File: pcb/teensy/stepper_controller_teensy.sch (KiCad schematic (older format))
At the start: 15 parts, among them P1 HEADER_02X08_SMD, SW1 SPST_SLIDE_AS, U1 TLE7230R

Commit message: Added L6470.
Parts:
- removed C2: 0.1uF, stepper_controller_teensy:SM1210, symbol 0.1uF
- removed L2, L3, L4, L5, L6, L7, L8, L9: LED_24V, stepper_controller_teensy:LED_555-3XXX, symbol LED_24V
- removed P1: HEADER_02X08_SMD, stepper_controller_teensy:HEADER_02x08_SMD, symbol HEADER_02X08_SMD
- removed U1: TLE7230R, stepper_controller_teensy:PG-DSO-36, symbol TLE7230R
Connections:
- net labels removed: OUT0, OUT1, OUT2, OUT3, OUT4, OUT5, OUT6, OUT7
- wire segments 85 -> 21
- no-connect marks 25 -> 23

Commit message: Added TERM_BLK_ANG_4_PIN.
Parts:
- added U?: L6470, footprints:POWERSO-36, symbol L6470
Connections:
- net labels added: BUSY, FLAG, OUT1A, OUT1B, OUT2A, OUT2B, SW
- net labels removed: PWM
- wire segments 21 -> 50
- no-connect marks 23 -> 24
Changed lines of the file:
@@
 NoConn ~ 3850 1150
 NoConn ~ 1350 1050
-NoConn ~ 1350 1450
 NoConn ~ 1350 1550
 NoConn ~ 1350 1650
@@
 RESET
 Text Label 1050 1350 0    60   ~ 0
-PWM
+FLAG
 $Comp
 L LED_24V L1
@@
 	1    0    0    -1
 $EndComp
+$Comp
+L L6470 U?
+U 1 1 57AA1BBB
+P 7200 3200
+F 0 "U?" H 7700 2300 60  0000 C CNN
+F 1 "L6470" H 6800 2300 60  0000 C CNN
+F 2 "footprints:POWERSO-36" H 7200 4850 60  0001 C CNN
+F 3 "" H 7600 3700 60  0000 C CNN
+F 4 "digikey" H 7200 4750 60  0001 C CNN "Vendor"
+F 5 "497-16432-1-ND" H 7200 4950 60  0001 C CNN "PartNumber"
+F 6 "Bipolar Motor Driver DMOS SPI PowerSO-36" H 7200 5050 60  0001 C CNN "Description"
+	1    7200 3200
+	1    0    0    -1
+$EndComp
+Wire Wire Line
+	6550 3250 6250 3250
+Wire Wire Line
+	6550 3350 6250 3350
+Wire Wire Line
+	6550 3450 6250 3450
+Wire Wire Line
+	6550 3550 6250 3550
+Text Label 6250 3450 0    60   ~ 0
+MISO
+Text Label 6250 3550 0    60   ~ 0
+MOSI
+Text Label 6250 3350 0    60   ~ 0
+SCK
+Text Label 6250 3250 0    60   ~ 0
+CS
+NoConn ~ 7850 3750
+NoConn ~ 6550 3750
+$Comp
+L GND #PWR?
+U 1 1 57AA211F
+P 7250 4300
+F 0 "#PWR?" H 7250 4050 50  0001 C CNN
+F 1 "GND" H 7255 4127 50  0000 C CNN
+F 2 "" H 7250 4300 50  0000 C CNN
+F 3 "" H 7250 4300 50  0000 C CNN
+	1    7250 4300
+	1    0    0    -1
+$EndComp
+Wire Wire Line
+	7050 4150 7050 4200
+Wire Wire Line
+	7050 4200 7450 4200
+Wire Wire Line
+	7450 4200 7450 4150
+Wire Wire Line
+	7150 4150 7150 4200
+Connection ~ 7150 4200
+Wire Wire Line
+	7250 4150 7250 4300
+Connection ~ 7250 4200
+Wire Wire Line
+	7350 4150 7350 4200
+Connection ~ 7350 4200
+Wire Wire Line
+	7850 2950 7950 2950
+Wire Wire Line
+	7850 3150 7950 3150
+Wire Wire Line
+	7850 3350 7950 3350
+Wire Wire Line
+	7850 3550 7950 3550
+Wire Wire Line
+	7850 3050 7900 3050
+Wire Wire Line
+	7900 3050 7900 2950
+Connection ~ 7900 2950
+Wire Wire Line
+	7850 3250 7900 3250
+Wire Wire Line
+	7900 3250 7900 3150
+Connection ~ 7900 3150
+Wire Wire Line
+	7850 3450 7900 3450
+Wire Wire Line
+	7900 3450 7900 3350
+Connection ~ 7900 3350
+Wire Wire Line
+	7850 3650 7900 3650
+Wire Wire Line
+	7900 3650 7900 3550
+Connection ~ 7900 3550
+Text Label 7950 2950 0    60   ~ 0
+OUT1A
+Text Label 7950 3150 0    60   ~ 0
+OUT2A
+Text Label 7950 3350 0    60   ~ 0
+OUT1B
+Text Label 7950 3550 0    60   ~ 0
+OUT2B
+Wire Wire Line
+	6550 3150 6250 3150
+Text Label 6250 3150 0    60   ~ 0
+RESET
+$Comp
+L GND #PWR?
+U 1 1 57AA2829
+P 6050 3100
+F 0 "#PWR?" H 6050 2850 50  0001 C CNN
+F 1 "GND" H 6055 2927 50  0000 C CNN
+F 2 "" H 6050 3100 50  0000 C CNN
+F 3 "" H 6050 3100 50  0000 C CNN
+	1    6050 3100
+	1    0    0    -1
+$EndComp
+Wire Wire Line
+	6550 3050 6050 3050
+Wire Wire Line
+	6050 3050 6050 3100
+Wire Wire Line
+	6550 2950 6250 2950
+Text Label 6250 2950 0    60   ~ 0
+BUSY
+Wire Wire Line
+	6550 2850 6250 2850
+Text Label 6250 2850 0    60   ~ 0
+FLAG
+Wire Wire Line
+	1350 1450 1050 1450
+Text Label 1050 1450 0    60   ~ 0
+BUSY
+Wire Wire Line
+	6550 3650 6250 3650
+Text Label 6250 3650 0    60   ~ 0
+SW
 $EndSCHEMATC

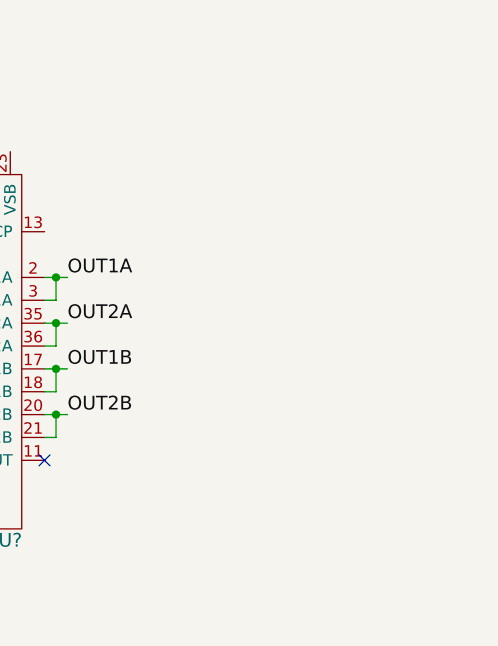
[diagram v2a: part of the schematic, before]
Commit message: Added terminal blocks.
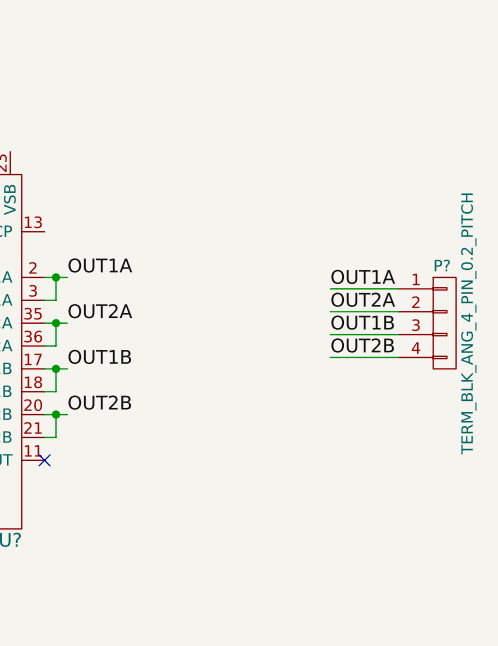
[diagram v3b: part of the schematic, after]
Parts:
- added P?: TERM_BLK_ANG_4_PIN_0.2_PITCH, footprints:TERM_BLK_ANG_4_PIN_0.2_PITCH, symbol TERM_BLK_ANG_4_PIN_0.2_PITCH
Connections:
- wire segments 50 -> 54
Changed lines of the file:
@@
 Text Label 6250 3650 0    60   ~ 0
 SW
+Wire Wire Line
+	9400 3000 9100 3000
+Wire Wire Line
+	9400 3100 9100 3100
+Wire Wire Line
+	9400 3200 9100 3200
+Wire Wire Line
+	9400 3300 9100 3300
+Text Label 9100 3000 0    60   ~ 0
+OUT1A
+Text Label 9100 3100 0    60   ~ 0
+OUT2A
+Text Label 9100 3200 0    60   ~ 0
+OUT1B
+Text Label 9100 3300 0    60   ~ 0
+OUT2B
+$Comp
+L TERM_BLK_ANG_4_PIN_0.2_PITCH P?
+U 1 1 57AA5C55
+P 9600 3150
+F 0 "P?" H 9550 3400 50  0000 L CNN
+F 1 "TERM_BLK_ANG_4_PIN_0.2_PITCH" V 9700 3150 50  0000 C CNN
+F 2 "footprints:TERM_BLK_ANG_4_PIN_0.2_PITCH" H 9500 3300 50  0001 C CNN
+F 3 "" H 9600 3150 50  0000 C CNN
+F 4 "digikey" H 9700 3500 60  0001 C CNN "Vendor"
+F 5 "A98350-ND" H 9800 3600 60  0001 C CNN "PartNumber"
+F 6 "TERM BLOCK 4POS 35DEG 5.08MM" H 9900 3700 60  0001 C CNN "Description"
+	1    9600 3150
+	1    0    0    -1
+$EndComp
 $EndSCHEMATC

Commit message: Added components and footprints.
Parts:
- removed C1: 10uF, stepper_controller_teensy:SM1210, symbol 10uF
- removed L1: LED_24V, stepper_controller_teensy:LED_555-3XXX, symbol LED_24V
- added SW?: KT_SWITCH, footprints:KT_SWITCH, symbol KT_SWITCH
- added T?: TERM_BLK_2_PIN_0.1_PITCH, footprints:TERM_BLK_2_PIN_0.1_PITCH, symbol TERM_BLK_2_PIN_0.1_PITCH
- added U?: MAX6817, footprints:MAX6817, symbol MAX6817
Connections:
- net labels added: +3.3V, SW_B
- net labels removed: VEE
- wire segments 54 -> 57
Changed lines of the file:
@@
 Wire Wire Line
 	1050 850  1350 850
-$Comp
-L VEE #PWR03
-U 1 1 57715626
-P 4350 800
-F 0 "#PWR03" H 4350 650 50  0001 C CNN
-F 1 "VEE" H 4367 973 50  0000 C CNN
-F 2 "" H 4350 800 50  0000 C CNN
-F 3 "" H 4350 800 50  0000 C CNN
-	1    4350 800
-	1    0    0    -1
-$EndComp
-Wire Wire Line
-	3850 950  4650 950
-Wire Wire Line
-	4350 950  4350 800
 NoConn ~ 3850 850
 NoConn ~ 3850 1050
-NoConn ~ 3850 1150
 NoConn ~ 1350 1050
 NoConn ~ 1350 1550
@@
 FLAG
 $Comp
-L LED_24V L1
-U 1 1 578D4B9A
-P 3700 3150
-F 0 "L1" H 3750 3250 50  0000 C CNN
-F 1 "LED_24V" H 3750 3050 50  0000 C CNN
-F 2 "stepper_controller_teensy:LED_555-3XXX" H 3600 3150 60  0001 C CNN
-F 3 "" H 3700 3150 60  0000 C CNN
-F 4 "digikey" H 3800 3350 60  0001 C CNN "Vendor"
-F 5 "350-1723-ND" H 3900 3450 60  0001 C CNN "PartNumber"
-F 6 "LED 2MM 24V VERTICAL RED PC MNT" H 4000 3550 60  0001 C CNN "Description"
-	1    3700 3150
-	0    1    1    0
-$EndComp
-$Comp
 L SPST_SLIDE_AS SW1
 U 1 1 578D4BFB
@@
 	0    1    1    0
 $EndComp
-$Comp
-L VDD #PWR07
-U 1 1 578D4F9D
-P 3100 2900
-F 0 "#PWR07" H 3100 2750 50  0001 C CNN
-F 1 "VDD" H 3117 3073 50  0000 C CNN
-F 2 "" H 3100 2900 50  0000 C CNN
-F 3 "" H 3100 2900 50  0000 C CNN
-	1    3100 2900
-	1    0    0    -1
-$EndComp
 Wire Wire Line
 	3100 2900 3100 2950
@@
 Text Label 3100 3550 0    60   ~ 0
 LED_PWR
-$Comp
-L GND #PWR08
-U 1 1 578D534F
-P 3700 3400
-F 0 "#PWR08" H 3700 3150 50  0001 C CNN
-F 1 "GND" H 3705 3227 50  0000 C CNN
-F 2 "" H 3700 3400 50  0000 C CNN
-F 3 "" H 3700 3400 50  0000 C CNN
-	1    3700 3400
-	1    0    0    -1
-$EndComp
-Wire Wire Line
-	3700 3350 3700 3400
-Wire Wire Line
-	3700 2950 3700 2850
-Text Label 3700 2850 0    60   ~ 0
-LED_PWR
-$Comp
-L 10uF C1
-U 1 1 578FA17B
-P 2500 3200
-F 0 "C1" H 2550 3300 40  0000 L CNN
-F 1 "10uF" H 2550 3100 30  0000 L CNN
-F 2 "stepper_controller_teensy:SM1210" H 2538 3050 30  0001 C CNN
-F 3 "" H 2500 3200 60  0000 C CNN
-F 4 "digikey" H 2600 3400 60  0001 C CNN "Vendor"
-F 5 "445-4536-1-ND" H 2700 3500 60  0001 C CNN "PartNumber"
-F 6 "CAP CER 10UF 50V 10% X7S 1210" H 2800 3600 60  0001 C CNN "Description"
-	1    2500 3200
-	1    0    0    -1
-$EndComp
-$Comp
-L GND #PWR09
-U 1 1 578FA28E
-P 2500 3450
-F 0 "#PWR09" H 2500 3200 50  0001 C CNN
-F 1 "GND" H 2505 3277 50  0000 C CNN
-F 2 "" H 2500 3450 50  0000 C CNN
-F 3 "" H 2500 3450 50  0000 C CNN
-	1    2500 3450
-	1    0    0    -1
-$EndComp
-$Comp
-L VDD #PWR010
-U 1 1 578FA2C6
-P 2500 2900
-F 0 "#PWR010" H 2500 2750 50  0001 C CNN
-F 1 "VDD" H 2517 3073 50  0000 C CNN
-F 2 "" H 2500 2900 50  0000 C CNN
-F 3 "" H 2500 2900 50  0000 C CNN
-	1    2500 2900
-	1    0    0    -1
-$EndComp
-Wire Wire Line
-	2500 2900 2500 3000
-Wire Wire Line
-	2500 3400 2500 3450
 $Comp
 L PWR_FLAG #FLG011
@@
 L PWR_FLAG #FLG013
 U 1 1 578F9241
-P 4650 800
-F 0 "#FLG013" H 4650 895 50  0001 C CNN
-F 1 "PWR_FLAG" H 4650 1024 50  0000 C CNN
-F 2 "" H 4650 800 50  0000 C CNN
-F 3 "" H 4650 800 50  0000 C CNN
-	1    4650 800
-	1    0    0    -1
-$EndComp
-Wire Wire Line
-	4650 950  4650 800
-Connection ~ 4350 950
+P 4400 1000
+F 0 "#FLG013" H 4400 1095 50  0001 C CNN
+F 1 "PWR_FLAG" H 4400 1224 50  0000 C CNN
+F 2 "" H 4400 1000 50  0000 C CNN
+F 3 "" H 4400 1000 50  0000 C CNN
+	1    4400 1000
+	1    0    0    -1
+$EndComp
 Wire Wire Line
 	1050 800  1050 850
@@
 	1    0    0    -1
 $EndComp
+$Comp
+L TERM_BLK_2_PIN_0.1_PITCH T?
+U 1 1 57AB3CB0
+P 9600 4400
+F 0 "T?" H 9600 4550 50  0000 C CNN
+F 1 "TERM_BLK_2_PIN_0.1_PITCH" V 9700 4400 50  0000 C CNN
+F 2 "footprints:TERM_BLK_2_PIN_0.1_PITCH" H 9500 4450 60  0001 C CNN
+F 3 "" H 9600 4400 60  0000 C CNN
+F 4 "digikey" H 9700 4650 60  0001 C CNN "Vendor"
+F 5 "A98333-ND" H 9800 4750 60  0001 C CNN "PartNumber"
+F 6 "TERM BLOCK 2POS SIDE ENT 2.54MM" H 9900 4850 60  0001 C CNN "Description"
+	1    9600 4400
+	1    0    0    -1
+$EndComp
+$Comp
+L GND #PWR?
+U 1 1 57AB53B5
+P 9350 4500
+F 0 "#PWR?" H 9350 4250 50  0001 C CNN
+F 1 "GND" H 9355 4327 50  0000 C CNN
+F 2 "" H 9350 4500 50  0000 C CNN
+F 3 "" H 9350 4500 50  0000 C CNN
+	1    9350 4500
+	1    0    0    -1
+$EndComp
+Text Label 1600 4400 0    60   ~ 0
+SW_B
+$Comp
+L KT_SWITCH SW?
+U 1 1 57AB5A65
+P 2250 5500
+F 0 "SW?" H 2250 5450 40  0000 C CNN
+F 1 "KT_SWITCH" H 2250 5600 40  0000 C CNN
+F 2 "footprints:KT_SWITCH" H 2150 5300 60  0001 C CNN
+F 3 "" H 2250 5450 60  0000 C CNN
+F 4 "digikey" H 2350 5700 60  0001 C CNN "Vendor"
+F 5 "CKN1860CT-ND" H 2450 5800 60  0001 C CNN "PartNumber"
+F 6 "SWITCH TACTILE SPST-NO 1VA 32V" H 2550 5900 60  0001 C CNN "Description"
+	1    2250 5500
+	0    1    1    0
+$EndComp
+Wire Wire Line
+	3800 4200 3800 4100
+Text Label 3800 4100 0    60   ~ 0
+SW_B
+$Comp
+L GND #PWR?
+U 1 1 57AB5E9F
+P 3800 4800
+F 0 "#PWR?" H 3800 4550 50  0001 C CNN
+F 1 "GND" H 3805 4627 50  0000 C CNN
+F 2 "" H 3800 4800 50  0000 C CNN
+F 3 "" H 3800 4800 50  0000 C CNN
+	1    3800 4800
+	1    0    0    -1
+$EndComp
+Wire Wire Line
+	3800 4700 3800 4800
+$Comp
+L MAX6817 U?
+U 1 1 57AB65A9
+P 2300 4650
+F 0 "U?" H 2300 5397 60  0000 C CNN
+F 1 "MAX6817" H 2300 5291 60  0000 C CNN
+F 2 "footprints:MAX6817" H 2450 4300 60  0001 C CNN
+F 3 "" H 2300 4650 60  0000 C CNN
+F 4 "digikey" H 2650 4500 60  0001 C CNN "Vendor"
+F 5 "MAX6817EUT+TCT-ND" H 2750 4600 60  0001 C CNN "PartNumber"
+F 6 "IC DEBOUNCER SWITCH DUAL SOT23-6" H 2850 4700 60  0001 C CNN "Description"
+	1    2300 4650
+	1    0    0    -1
+$EndComp
+Wire Wire Line
+	1600 4400 1900 4400
+Wire Wire Line
+	2700 4400 2800 4400
+Text Label 2800 4400 0    60   ~ 0
+SW
+Wire Wire Line
+	9400 4350 9100 4350
+Text Label 9100 4350 0    60   ~ 0
+SW_B
+Wire Wire Line
+	9400 4450 9350 4450
+Wire Wire Line
+	9350 4450 9350 4500
+NoConn ~ 3850 950
+$Comp
+L +3.3V #PWR?
+U 1 1 57AB7183
+P 4150 1050
+F 0 "#PWR?" H 4150 900 50  0001 C CNN
+F 1 "+3.3V" H 4165 1223 50  0000 C CNN
+F 2 "" H 4150 1050 50  0000 C CNN
+F 3 "" H 4150 1050 50  0000 C CNN
+	1    4150 1050
+	1    0    0    -1
+$EndComp
+Wire Wire Line
+	4400 1000 4400 1150
+Wire Wire Line
+	4400 1150 3850 1150
+Wire Wire Line
+	4150 1050 4150 1150
+Connection ~ 4150 1150
+$Comp
+L +3.3V #PWR?
+U 1 1 57AB7329
+P 3100 2900
+F 0 "#PWR?" H 3100 2750 50  0001 C CNN
+F 1 "+3.3V" H 3115 3073 50  0000 C CNN
+F 2 "" H 3100 2900 50  0000 C CNN
+F 3 "" H 3100 2900 50  0000 C CNN
+	1    3100 2900
+	1    0    0    -1
+$EndComp

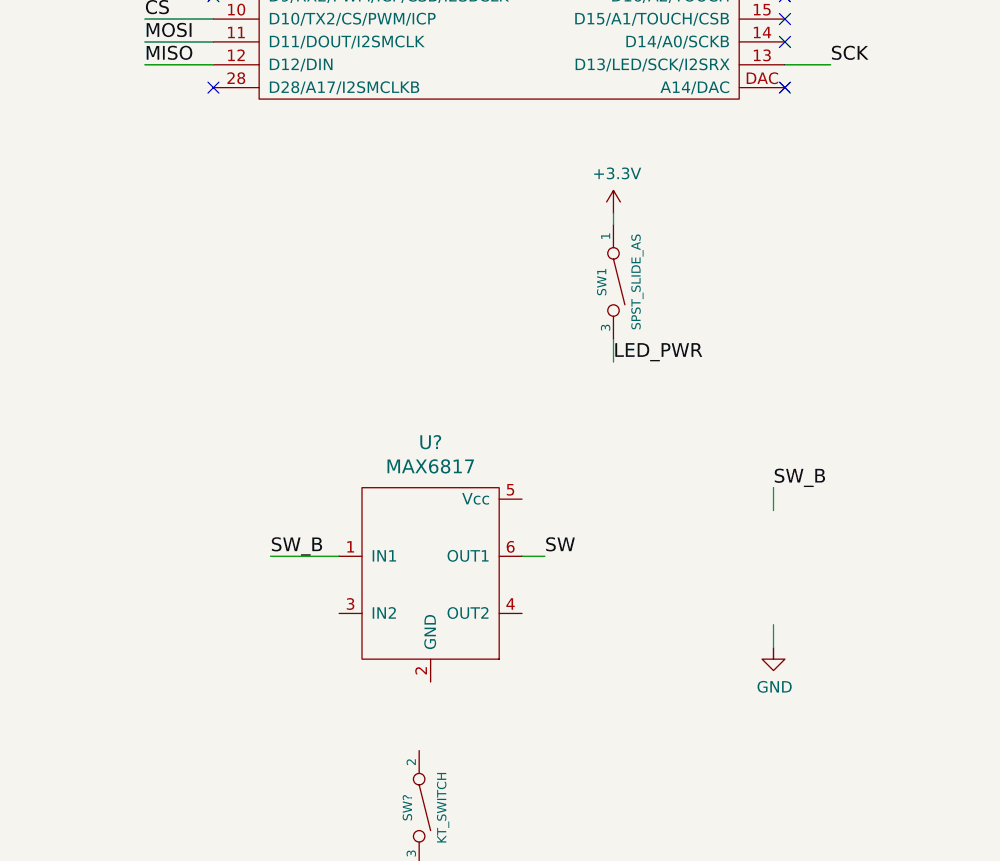
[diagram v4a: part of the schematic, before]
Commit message: Added resistors.
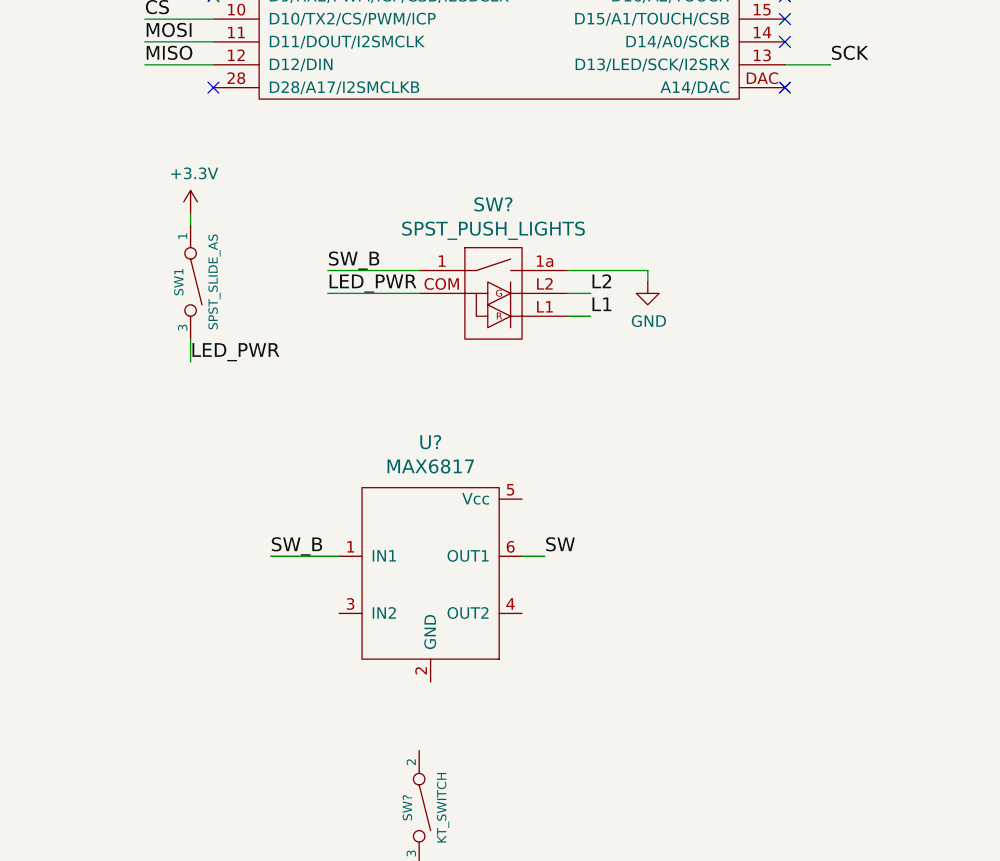
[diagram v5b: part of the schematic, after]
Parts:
- added SW?: SPST_PUSH_LIGHTS, footprints:KP_SWITCH, symbol SPST_PUSH_LIGHTS
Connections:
- net GND: now also SW?.1a
- net LED_PWR: now also SW?.COM
- net SW_B: now also SW?.1
- new net L1: SW?.L1
- new net L2: SW?.L2
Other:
- moved on the sheet: SW1
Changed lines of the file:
@@
 L SPST_SLIDE_AS SW1
 U 1 1 578D4BFB
-P 3100 3200
-F 0 "SW1" H 3100 3150 40  0000 C CNN
-F 1 "SPST_SLIDE_AS" H 3100 3300 40  0000 C CNN
-F 2 "stepper_controller_teensy:SPST_SLIDE_AS" H 3000 3000 60  0001 C CNN
-F 3 "" H 3100 3200 60  0000 C CNN
-F 4 "digikey" H 3200 3400 60  0001 C CNN "Vendor"
-F 5 "360-2610-ND" H 3300 3500 60  0001 C CNN "PartNumber"
-F 6 "SWITCH SLIDE SPST 0.4VA 28V" H 3400 3600 60  0001 C CNN "Description"
-	1    3100 3200
+P 1250 3200
+F 0 "SW1" H 1250 3150 40  0000 C CNN
+F 1 "SPST_SLIDE_AS" H 1250 3300 40  0000 C CNN
+F 2 "stepper_controller_teensy:SPST_SLIDE_AS" H 1150 3000 60  0001 C CNN
+F 3 "" H 1250 3200 60  0000 C CNN
+F 4 "digikey" H 1350 3400 60  0001 C CNN "Vendor"
+F 5 "360-2610-ND" H 1450 3500 60  0001 C CNN "PartNumber"
+F 6 "SWITCH SLIDE SPST 0.4VA 28V" H 1550 3600 60  0001 C CNN "Description"
+	1    1250 3200
 	0    1    1    0
 $EndComp
 Wire Wire Line
-	3100 2900 3100 2950
-Wire Wire Line
-	3100 3450 3100 3550
-Text Label 3100 3550 0    60   ~ 0
+	1250 2900 1250 2950
+Wire Wire Line
+	1250 3450 1250 3550
+Text Label 1250 3550 0    60   ~ 0
 LED_PWR
 $Comp
@@
 	0    1    1    0
 $EndComp
-Wire Wire Line
-	3800 4200 3800 4100
-Text Label 3800 4100 0    60   ~ 0
+Text Label 1850 3150 0    60   ~ 0
 SW_B
 $Comp
 L GND #PWR?
 U 1 1 57AB5E9F
-P 3800 4800
-F 0 "#PWR?" H 3800 4550 50  0001 C CNN
-F 1 "GND" H 3805 4627 50  0000 C CNN
-F 2 "" H 3800 4800 50  0000 C CNN
-F 3 "" H 3800 4800 50  0000 C CNN
-	1    3800 4800
-	1    0    0    -1
-$EndComp
-Wire Wire Line
-	3800 4700 3800 4800
+P 3250 3200
+F 0 "#PWR?" H 3250 2950 50  0001 C CNN
+F 1 "GND" H 3255 3027 50  0000 C CNN
+F 2 "" H 3250 3200 50  0000 C CNN
+F 3 "" H 3250 3200 50  0000 C CNN
+	1    3250 3200
+	1    0    0    -1
+$EndComp
 $Comp
 L MAX6817 U?
@@
 L +3.3V #PWR?
 U 1 1 57AB7329
-P 3100 2900
-F 0 "#PWR?" H 3100 2750 50  0001 C CNN
-F 1 "+3.3V" H 3115 3073 50  0000 C CNN
-F 2 "" H 3100 2900 50  0000 C CNN
-F 3 "" H 3100 2900 50  0000 C CNN
-	1    3100 2900
-	1    0    0    -1
-$EndComp
+P 1250 2900
+F 0 "#PWR?" H 1250 2750 50  0001 C CNN
+F 1 "+3.3V" H 1265 3073 50  0000 C CNN
+F 2 "" H 1250 2900 50  0000 C CNN
+F 3 "" H 1250 2900 50  0000 C CNN
+	1    1250 2900
+	1    0    0    -1
+$EndComp
+$Comp
+L SPST_PUSH_LIGHTS SW?
+U 1 1 57AB858A
+P 2550 3250
+F 0 "SW?" H 2575 3637 60  0000 C CNN
+F 1 "SPST_PUSH_LIGHTS" H 2575 3531 60  0000 C CNN
+F 2 "footprints:KP_SWITCH" H 2450 2900 60  0001 C CNN
+F 3 "" H 2550 3250 60  0001 C CNN
+F 4 "digikey" H 2650 3100 60  0001 C CNN "Vendor"
+F 5 "360-2461-ND" H 2750 3200 60  0001 C CNN "PartNumber"
+F 6 "Pushbutton Switch SPST-NO Standard Illuminated Through Hole" H 2850 3300 60  0001 C CNN "Description"
+	1    2550 3250
+	1    0    0    -1
+$EndComp
+Wire Wire Line
+	2250 3250 1850 3250
+Wire Wire Line
+	2250 3150 1850 3150
+Text Label 1850 3250 0    60   ~ 0
+LED_PWR
+Wire Wire Line
+	2900 3250 3000 3250
+Wire Wire Line
+	2900 3350 3000 3350
+Text Label 3000 3250 0    60   ~ 0
+L2
+Text Label 3000 3350 0    60   ~ 0
+L1
+Wire Wire Line
+	2900 3150 3250 3150
+Wire Wire Line
+	3250 3150 3250 3200
 $EndSCHEMATC
